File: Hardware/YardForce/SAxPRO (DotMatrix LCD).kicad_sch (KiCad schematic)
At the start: 21 parts, among them U1 AMS1117-3.3

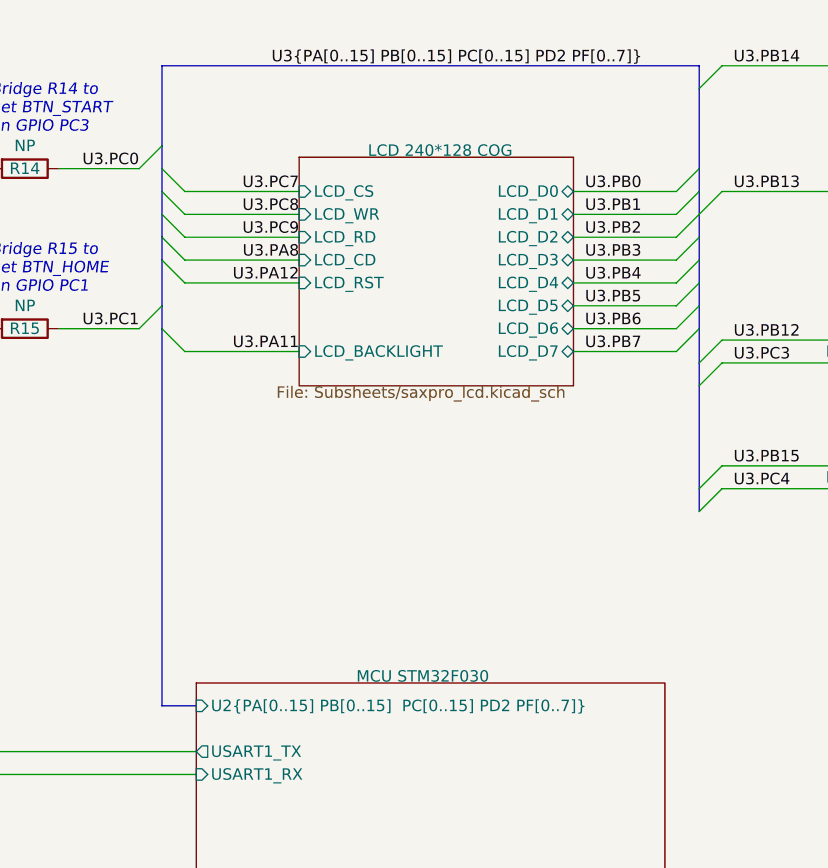
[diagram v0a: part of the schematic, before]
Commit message: Add touch panel
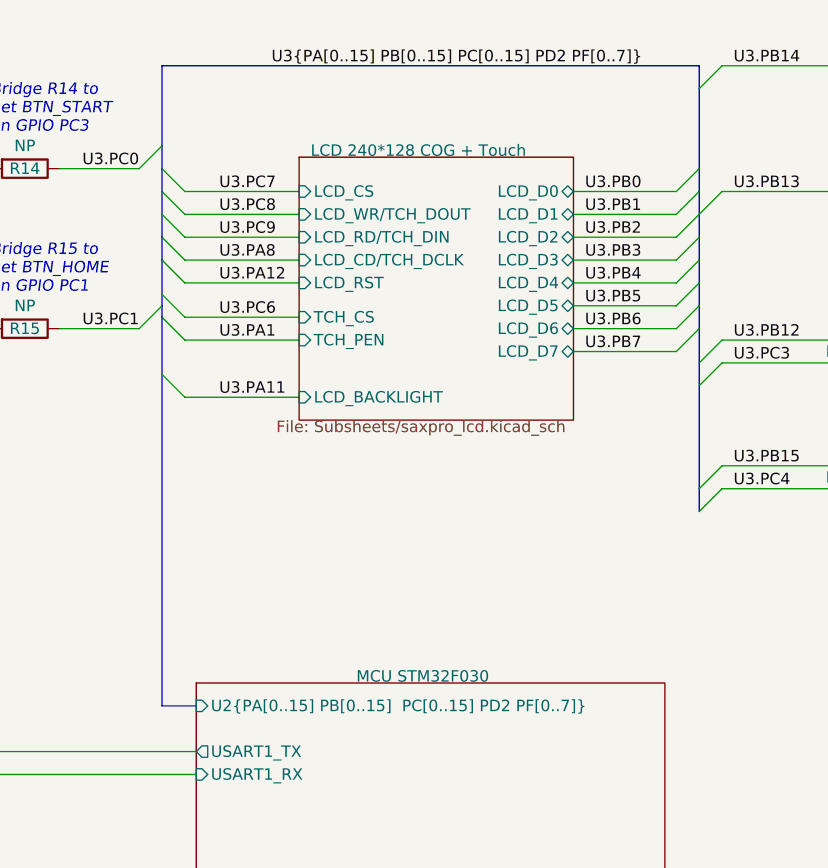
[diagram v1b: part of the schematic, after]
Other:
- sheet LCD 240*128 COG renamed LCD 240*128 COG + Touch
- sheet LCD 240*128 COG + Touch ports: added LCD_CD/TCH_DCLK, LCD_RD/TCH_DIN, LCD_WR/TCH_DOUT, TCH_CS, TCH_PEN; removed LCD_CD, LCD_RD, LCD_WR

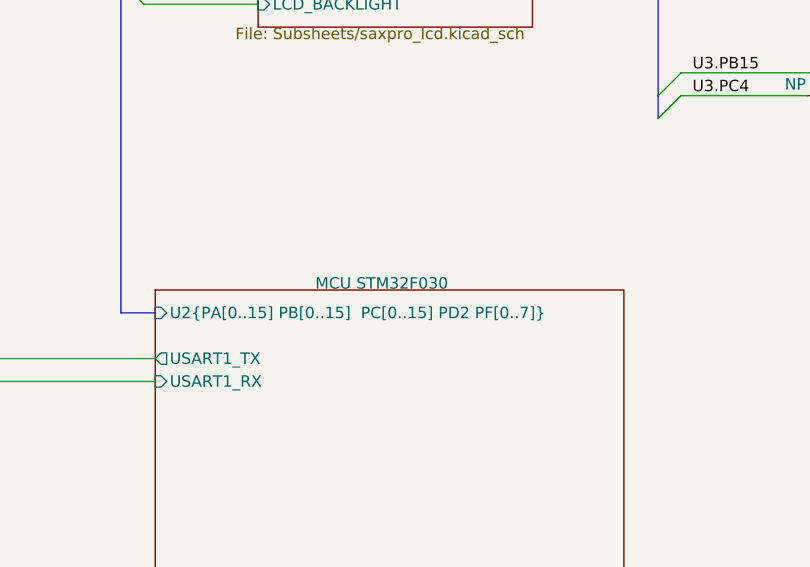
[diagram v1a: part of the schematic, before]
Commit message: Add flash and some cleanup
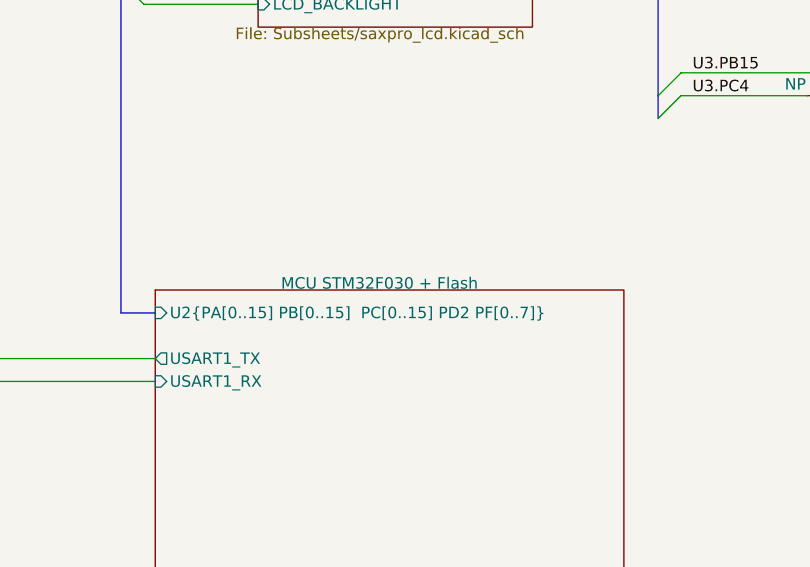
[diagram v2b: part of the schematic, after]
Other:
- sheet MCU STM32F030 renamed MCU STM32F030 + Flash
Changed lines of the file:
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@@
     (stroke (width 0.1524) (type solid) (color 0 0 0 0))
     (fill (color 0 0 0 0.0000))
-    (property "Sheet name" "MCU STM32F030" (id 0) (at 176.53 88.9 0)
+    (property "Sheet name" "MCU STM32F030 + Flash" (id 0) (at 172.72 88.9 0)
       (effects (font (size 1.27 1.27)) (justify left bottom))
     )
@@
       (reference "#PWR?") (unit 1) (value "+3.3V") (footprint "")
     )
+    (path "/32dee119-3232-4883-92dd-b6a76c2a2576/8c3e7104-aa64-42e5-84e0-e6cc833b580c"
+      (reference "#PWR?") (unit 1) (value "GND") (footprint "")
+    )
+    (path "/cce85892-34db-41da-93ff-f2d70e2cec22/8c3e7104-aa64-42e5-84e0-e6cc833b580c"
+      (reference "#PWR?") (unit 1) (value "GND") (footprint "")
+    )
+    (path "/38d2f403-0b05-41d5-9367-693053e593f2/8c3e7104-aa64-42e5-84e0-e6cc833b580c"
+      (reference "#PWR?") (unit 1) (value "GND") (footprint "")
+    )
     (path "/f943ab76-06db-4228-8039-ceb5eee988d2/8c3e7104-aa64-42e5-84e0-e6cc833b580c"
       (reference "#PWR?") (unit 1) (value "GND") (footprint "")
     )
-    (path "/38d2f403-0b05-41d5-9367-693053e593f2/8c3e7104-aa64-42e5-84e0-e6cc833b580c"
-      (reference "#PWR?") (unit 1) (value "GND") (footprint "")
-    )
-    (path "/cce85892-34db-41da-93ff-f2d70e2cec22/8c3e7104-aa64-42e5-84e0-e6cc833b580c"
-      (reference "#PWR?") (unit 1) (value "GND") (footprint "")
-    )
-    (path "/32dee119-3232-4883-92dd-b6a76c2a2576/8c3e7104-aa64-42e5-84e0-e6cc833b580c"
+    (path "/bb04b720-fddd-43a5-b689-bd08749bb66d/8c3e7104-aa64-42e5-84e0-e6cc833b580c"
       (reference "#PWR?") (unit 1) (value "GND") (footprint "")
     )
     (path "/ac3e26fc-5bee-413c-8a13-d3e2f8176b67/8c3e7104-aa64-42e5-84e0-e6cc833b580c"
-      (reference "#PWR?") (unit 1) (value "GND") (footprint "")
-    )
-    (path "/bb04b720-fddd-43a5-b689-bd08749bb66d/8c3e7104-aa64-42e5-84e0-e6cc833b580c"
       (reference "#PWR?") (unit 1) (value "GND") (footprint "")
     )
@@
       (reference "D4") (unit 1) (value "D") (footprint "")
     )
-    (path "/bb04b720-fddd-43a5-b689-bd08749bb66d/39abff33-50ea-4971-a0a3-b359beb69394"
+    (path "/ac3e26fc-5bee-413c-8a13-d3e2f8176b67/39abff33-50ea-4971-a0a3-b359beb69394"
       (reference "D?") (unit 1) (value "D") (footprint "")
     )
@@
       (reference "D?") (unit 1) (value "D") (footprint "")
     )
-    (path "/cce85892-34db-41da-93ff-f2d70e2cec22/39abff33-50ea-4971-a0a3-b359beb69394"
-      (reference "D?") (unit 1) (value "D") (footprint "")
-    )
-    (path "/ac3e26fc-5bee-413c-8a13-d3e2f8176b67/39abff33-50ea-4971-a0a3-b359beb69394"
-      (reference "D?") (unit 1) (value "D") (footprint "")
-    )
     (path "/98ec378d-9cd0-45fd-882c-58a94a607bdf/f3169df7-c84c-4574-887e-9b30698ba6a5"
       (reference "D?") (unit 1) (value "LED_Backlight") (footprint "")
@@
       (reference "JP7") (unit 1) (value "Conn_01x08_Female") (footprint "")
     )
+    (path "/cce85892-34db-41da-93ff-f2d70e2cec22/39abff33-50ea-4971-a0a3-b359beb69394"
+      (reference "NP") (unit 1) (value "D") (footprint "")
+    )
+    (path "/bb04b720-fddd-43a5-b689-bd08749bb66d/39abff33-50ea-4971-a0a3-b359beb69394"
+      (reference "NP") (unit 1) (value "D") (footprint "")
+    )
     (path "/98ec378d-9cd0-45fd-882c-58a94a607bdf/4d62c368-251e-43c6-b114-b4cc2109e592"
       (reference "Q1") (unit 1) (value "Q_NPN_BEC") (footprint "")
@@
       (reference "Rb1") (unit 1) (value "4R7") (footprint "")
     )
+    (path "/cce85892-34db-41da-93ff-f2d70e2cec22/f3b812c2-a0fc-4a10-813c-b7868a9843a7"
+      (reference "S1") (unit 1) (value "BTN") (footprint "")
+    )
+    (path "/bb04b720-fddd-43a5-b689-bd08749bb66d/f3b812c2-a0fc-4a10-813c-b7868a9843a7"
+      (reference "S2") (unit 1) (value "BTN") (footprint "")
+    )
     (path "/ac3e26fc-5bee-413c-8a13-d3e2f8176b67/f3b812c2-a0fc-4a10-813c-b7868a9843a7"
       (reference "S3") (unit 1) (value "BTN") (footprint "")
     )
-    (path "/bb04b720-fddd-43a5-b689-bd08749bb66d/f3b812c2-a0fc-4a10-813c-b7868a9843a7"
-      (reference "S?") (unit 1) (value "BTN") (footprint "")
-    )
     (path "/32dee119-3232-4883-92dd-b6a76c2a2576/f3b812c2-a0fc-4a10-813c-b7868a9843a7"
       (reference "S?") (unit 1) (value "BTN") (footprint "")
@@
       (reference "S?") (unit 1) (value "BTN") (footprint "")
     )
-    (path "/cce85892-34db-41da-93ff-f2d70e2cec22/f3b812c2-a0fc-4a10-813c-b7868a9843a7"
-      (reference "S?") (unit 1) (value "BTN") (footprint "")
-    )
     (path "/395e2a64-9334-4df7-8ce2-0c2b64ad8634"
       (reference "U1") (unit 1) (value "AMS1117-3.3") (footprint "Package_TO_SOT_SMD:SOT-223-3_TabPin2")
@@
       (reference "U3") (unit 1) (value "STM32F030RCTx") (footprint "Package_QFP:LQFP-64_10x10mm_P0.5mm")
     )
-  )
+    (path "/6f8d9ecb-cf0e-4216-a06b-57d9741d7238/f7fa3a72-bcbb-49cc-8ab0-92c04ed847b1"
+      (reference "U4") (unit 1) (value "SST25VF512A") (footprint "Package_SO:SOP-8_3.9x4.9mm_P1.27mm")
+    )
+  )
